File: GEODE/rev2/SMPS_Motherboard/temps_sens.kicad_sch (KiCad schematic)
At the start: 1 part, among them U1501 MCP9700BT-E/TT

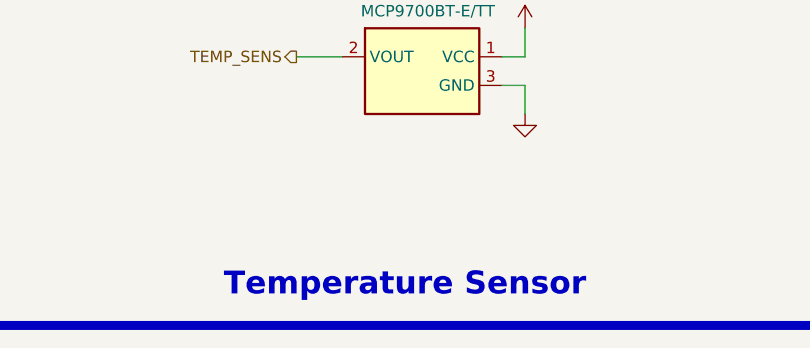
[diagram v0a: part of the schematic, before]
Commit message: changed connectors, removed can, added fuse, disconnected EXTVCC in power generation
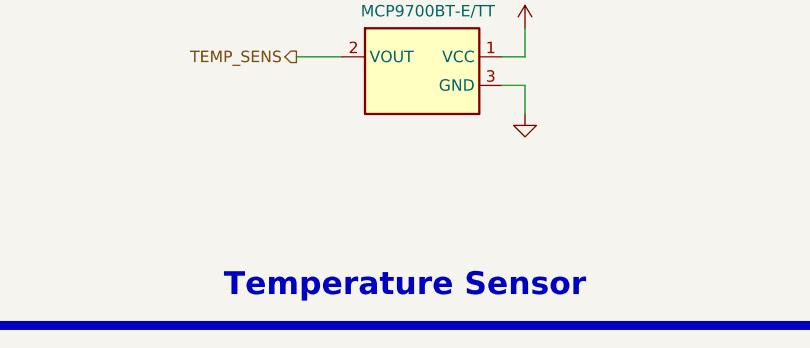
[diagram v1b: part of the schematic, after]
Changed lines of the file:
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@@
 (kicad_sch
-	(version 20231120)
+	(version 20250114)
 	(generator "eeschema")
-	(generator_version "8.0")
+	(generator_version "9.0")
 	(paper "A5")
+	(rectangle
+		(start 44.45 32.385)
+		(end 171.45 88.9)
+		(stroke
+			(width 1)
+			(type default)
+			(color 200 200 200 1)
+		)
+		(fill
+			(type none)
+		)
+	)
+	(text_box "[18] Interface - Temperature Sensor\n\n"
+		(exclude_from_sim no)
+		(at 12.065 15.24 0)
+		(size 186.055 12.7)
+		(margins 4.4999 4.4999 4.4999 4.4999)
+		(stroke
+			(width -0.0001)
+			(type default)
+		)
+		(fill
+			(type none)
+		)
+		(effects
+			(font
+				(face "Times New Roman")
+				(size 6 6)
+				(thickness 1.2)
+				(bold yes)
+				(color 162 22 34 1)
+			)
+		)
+	)
+	(text_box "Temperature Sensor\n"
+		(exclude_from_sim no)
+		(at 44.45 78.105 0)
+		(size 127 9.525)
+		(margins 1.9049 1.9049 1.9049 1.9049)
+		(stroke
+			(width -0.0001)
+			(type default)
+		)
+		(fill
+			(type none)
+		)
+		(effects
+			(font
+				(face "Times New Roman")
+				(size 2.54 2.54)
+				(thickness 0.508)
+				(bold yes)
+				(color 162 22 34 1)
+			)
+			(justify bottom)
+		)
+	)
 	(wire
 		(pts
@@
 		)
 	)
-	(rectangle
-		(start 44.45 32.385)
-		(end 171.45 88.9)
-		(stroke
-			(width 1)
-			(type default)
-			(color 200 200 200 1)
-		)
-		(fill
-			(type none)
-		)
-	)
-	(text_box "[18] Interface - Temperature Sensor\n\n"
-		(exclude_from_sim no)
-		(at 12.065 15.24 0)
-		(size 186.055 12.7)
-		(stroke
-			(width -0.0001)
-			(type default)
-		)
-		(fill
-			(type none)
-		)
-		(effects
-			(font
-				(face "Times New Roman")
-				(size 6 6)
-				(thickness 1.2)
-				(bold yes)
-				(color 162 22 34 1)
-			)
-		)
-	)
-	(text_box "Temperature Sensor\n"
-		(exclude_from_sim no)
-		(at 44.45 78.105 0)
-		(size 127 9.525)
-		(stroke
-			(width -0.0001)
-			(type default)
-		)
-		(fill
-			(type none)
-		)
-		(effects
-			(font
-				(face "Times New Roman")
-				(size 2.54 2.54)
-				(thickness 0.508)
-				(bold yes)
-				(color 162 22 34 1)
-			)
-			(justify bottom)
-		)
-	)
 	(hierarchical_label "TEMP_SENS"
 		(shape output)
 		(at 95.885 59.055 180)
-		(fields_autoplaced yes)
 		(effects
 			(font
